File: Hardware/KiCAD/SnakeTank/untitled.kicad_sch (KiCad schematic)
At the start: 2 parts, among them J3 RJ45

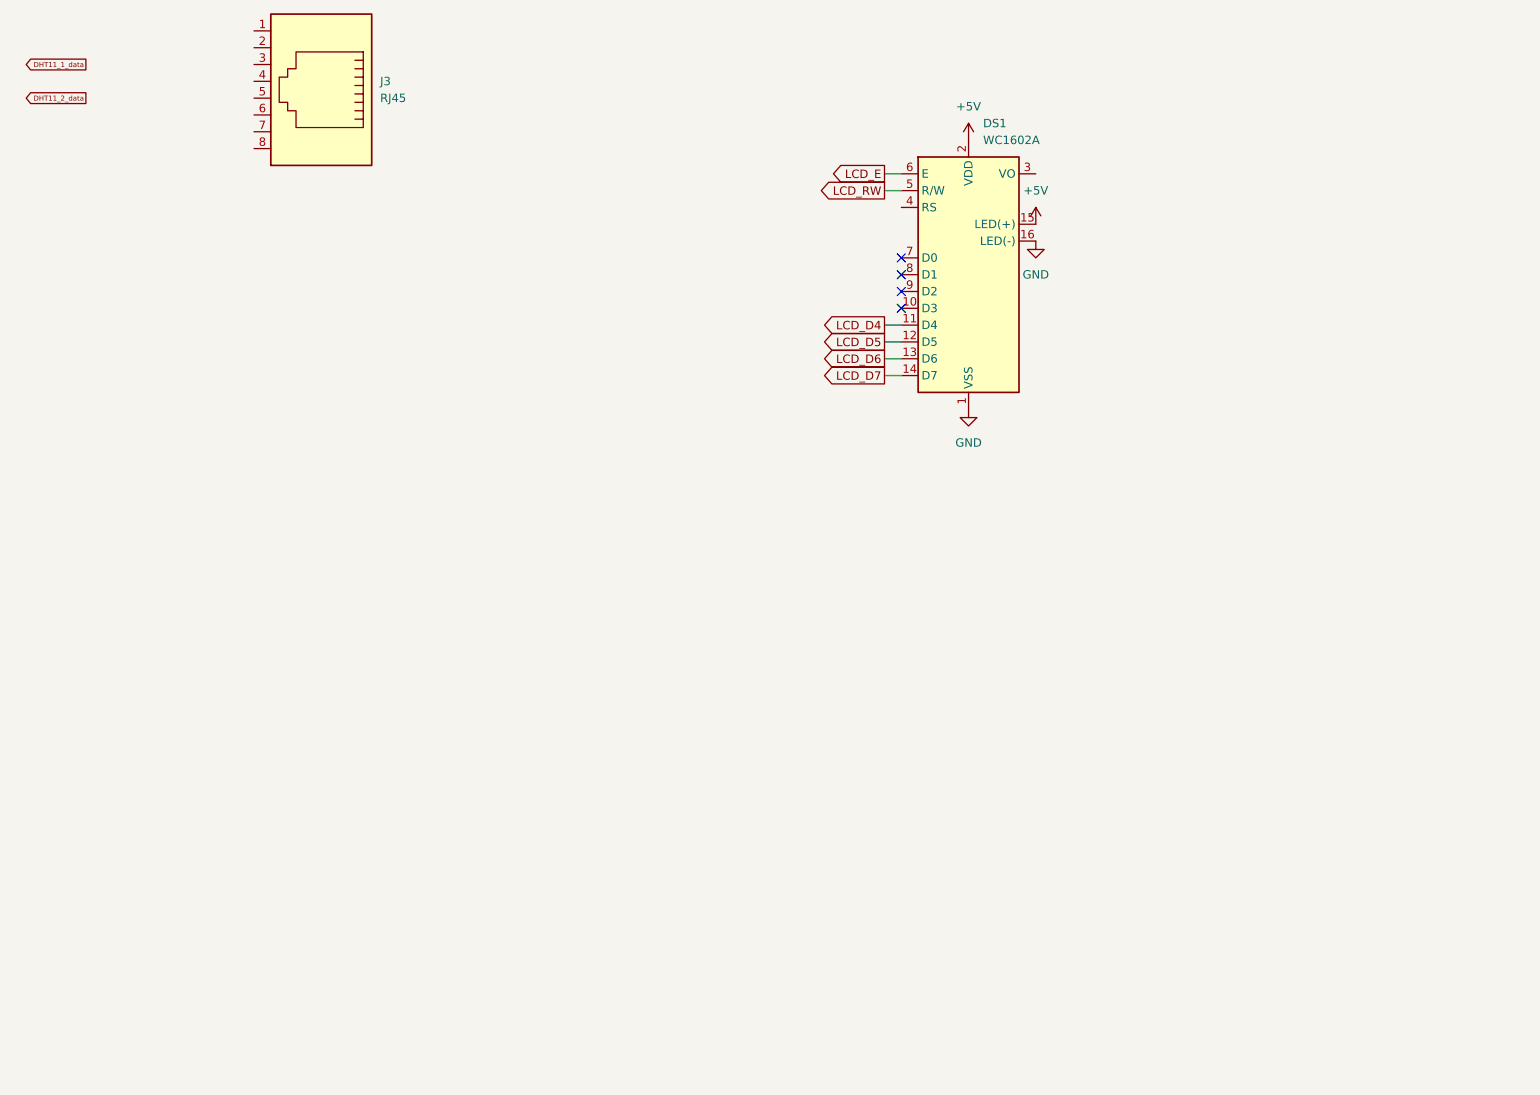
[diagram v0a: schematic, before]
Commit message: Updated schematic and export PDF
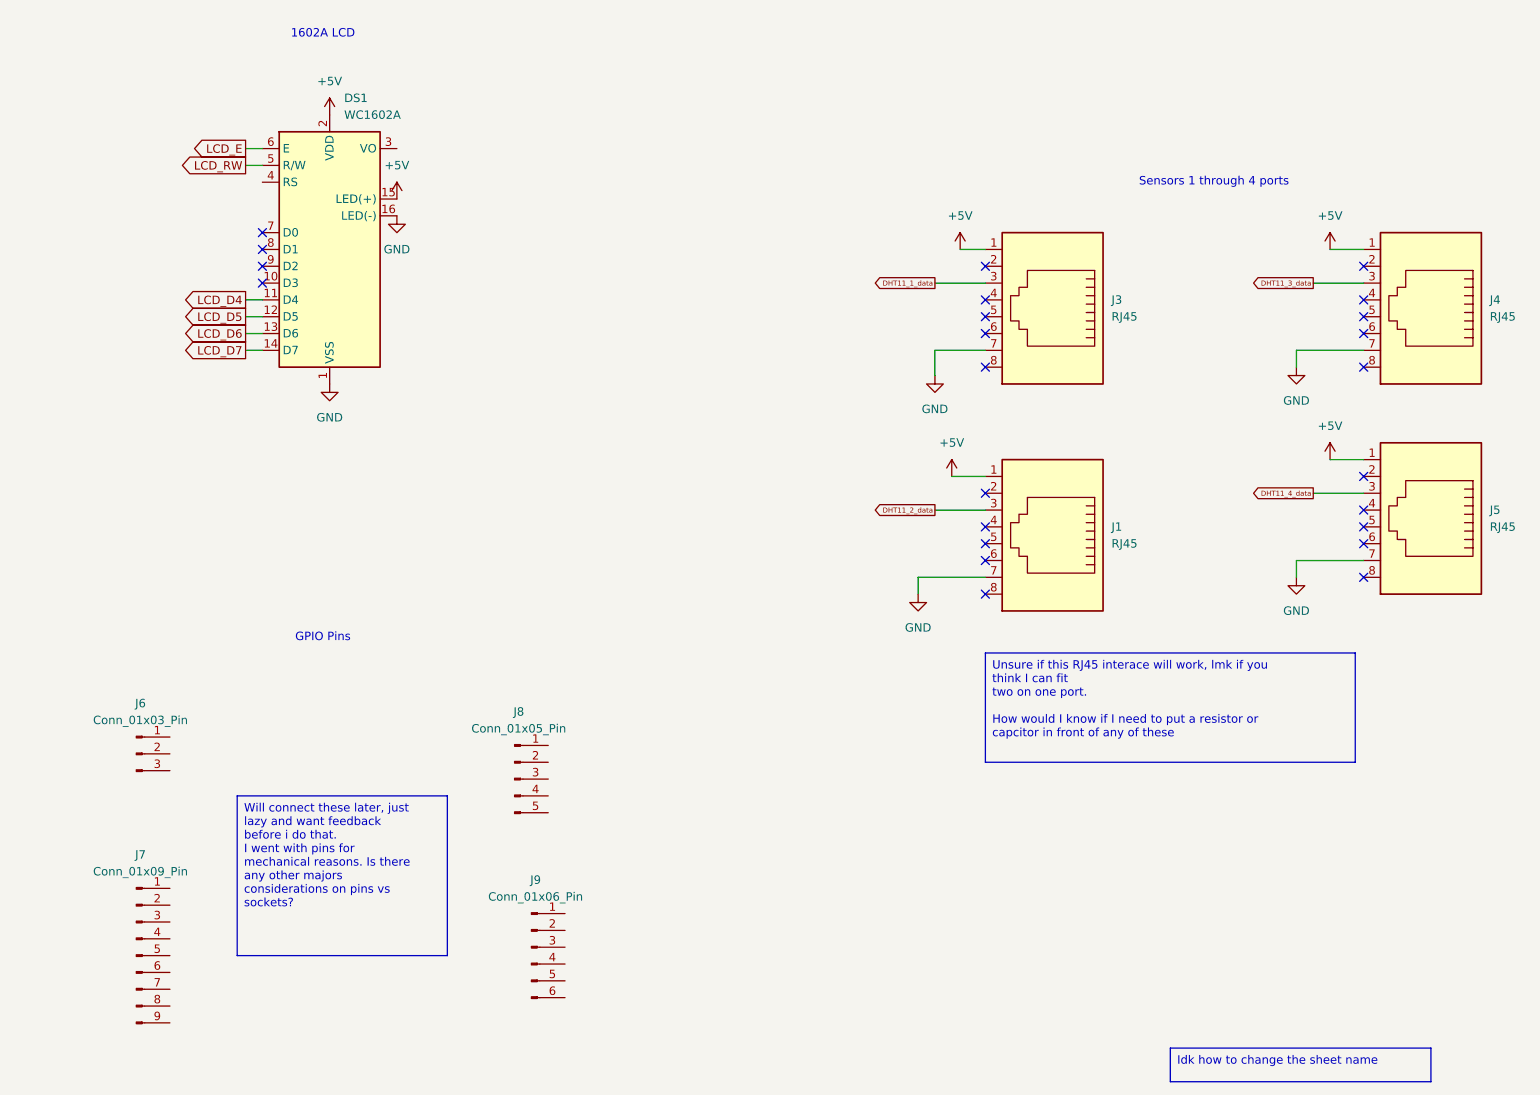
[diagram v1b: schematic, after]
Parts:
- added J1, J4, J5: RJ45, symbol Connector:RJ45
- added J6: Conn_01x03_Pin, symbol Connector:Conn_01x03_Pin
- added J7: Conn_01x09_Pin, symbol Connector:Conn_01x09_Pin
- added J8: Conn_01x05_Pin, symbol Connector:Conn_01x05_Pin
- added J9: Conn_01x06_Pin, symbol Connector:Conn_01x06_Pin
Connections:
- net +5V: now also J3.1, J1.1, J4.1, J5.1
- net DHT11_1_data: now also J3.3
- net DHT11_2_data: now also J1.3
- net GND: now also J3.7, J1.7, J4.7, J5.7
- new net DHT11_3_data: J4.3
- new net DHT11_4_data: J5.3
- no-connect marks 4 -> 24
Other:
- note added: "1602A LCD"
- note added: "GPIO Pins"
- note added: "Sensors 1 through 4 ports"
- moved on the sheet: DS1, J3
